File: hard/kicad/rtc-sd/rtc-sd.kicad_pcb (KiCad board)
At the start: 2 copper layers, 53.3 x 130.8 mm, 38 parts, among them J1 SIDECAR, J2 SD0, J3 SD1, J4 SPI2, J5 SPI3, J6 RTC, J7 EXPANSION, Q1 2N7000, U1 74HC138, U2 74HC174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

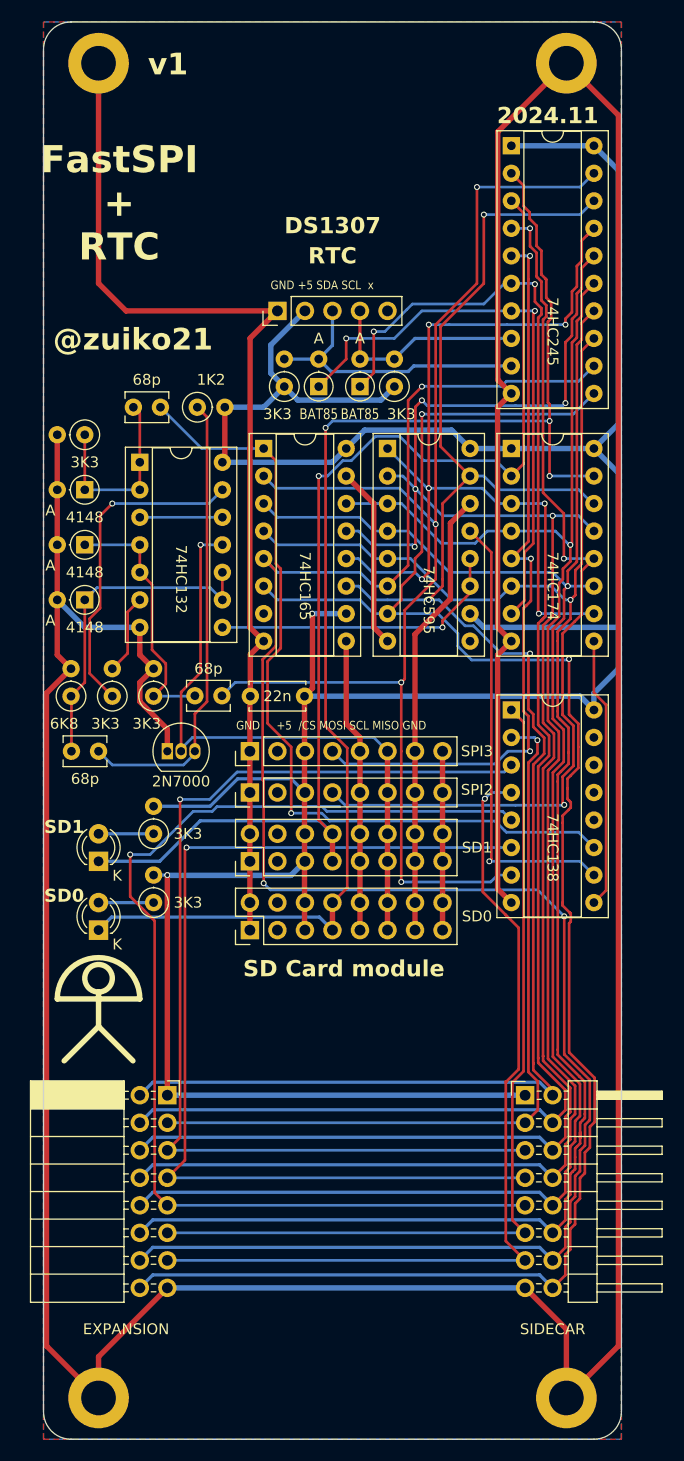
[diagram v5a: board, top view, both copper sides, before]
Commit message: add limits to rtc-sd
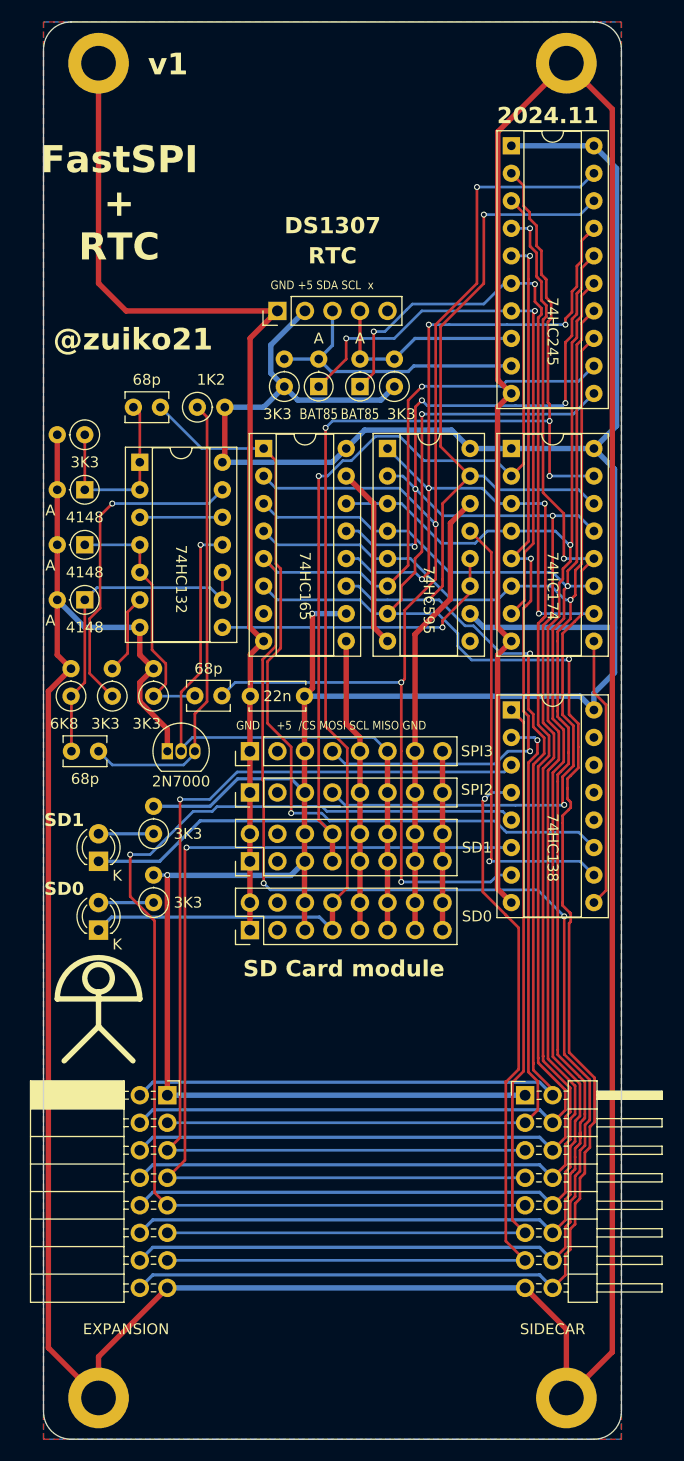
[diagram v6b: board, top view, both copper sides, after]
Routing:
- net +5V: track 288.7 -> 287.9 mm
- net GND: track 512.5 -> 511.8 mm
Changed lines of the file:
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@@
 		)
 		(property "Value" "SD1"
-			(at 3.175 -3.175 0)
+			(at 3.81 -3.175 0)
 			(unlocked yes)
 			(layer "F.SilkS")
@@
 		)
 		(property "Value" "SD0"
-			(at 3.175 -3.175 0)
+			(at 3.81 -3.175 0)
 			(unlocked yes)
 			(layer "F.SilkS")
@@
 	)
 	(segment
-		(start 73.66 152.4)
-		(end 78.465 147.595)
+		(start 68.58 59.69)
+		(end 67.33 58.44)
 		(width 0.5)
 		(layer "F.Cu")
@@
 	)
 	(segment
-		(start 68.58 59.69)
-		(end 67.33 58.44)
+		(start 67.31 60.96)
+		(end 67.31 81.28)
 		(width 0.5)
 		(layer "F.Cu")
@@
 	)
 	(segment
-		(start 67.31 60.96)
-		(end 67.31 81.28)
+		(start 25.85 147.77)
+		(end 25.85 87.18)
 		(width 0.5)
 		(layer "F.Cu")
@@
 	)
 	(segment
-		(start 27.94 85.09)
-		(end 25.675 87.355)
+		(start 25.85 87.18)
+		(end 27.94 85.09)
 		(width 0.5)
 		(layer "F.Cu")
@@
 	)
 	(segment
-		(start 78.465 34.015)
-		(end 73.66 29.21)
+		(start 68.58 59.69)
+		(end 67.31 60.96)
 		(width 0.5)
 		(layer "F.Cu")
@@
 	)
 	(segment
-		(start 68.58 59.69)
-		(end 67.31 60.96)
+		(start 77.9 148.16)
+		(end 77.9 33.45)
 		(width 0.5)
 		(layer "F.Cu")
@@
 	)
 	(segment
-		(start 44.47 54.59)
-		(end 44.47 64.75)
+		(start 30.48 152.4)
+		(end 25.85 147.77)
 		(width 0.5)
 		(layer "F.Cu")
@@
 	)
 	(segment
-		(start 25.675 87.355)
-		(end 25.675 147.595)
+		(start 44.47 54.59)
+		(end 44.47 64.75)
 		(width 0.5)
 		(layer "F.Cu")
@@
 	)
 	(segment
+		(start 77.9 33.45)
+		(end 73.66 29.21)
+		(width 0.5)
+		(layer "F.Cu")
+		(net 1)
+	)
+	(segment
 		(start 73.66 146.05)
 		(end 73.66 152.4)
@@
 	)
 	(segment
-		(start 25.675 147.595)
-		(end 30.48 152.4)
-		(width 0.5)
-		(layer "F.Cu")
-		(net 1)
-	)
-	(segment
 		(start 62.23 109.22)
 		(end 62.23 92.71)
@@
 	)
 	(segment
+		(start 73.66 152.4)
+		(end 77.9 148.16)
+		(width 0.5)
+		(layer "F.Cu")
+		(net 1)
+	)
+	(segment
 		(start 30.48 148.59)
 		(end 30.48 152.4)
@@
 	)
 	(segment
-		(start 78.465 147.595)
-		(end 78.465 34.015)
-		(width 0.5)
-		(layer "F.Cu")
-		(net 1)
-	)
-	(segment
 		(start 68.58 82.55)
 		(end 67.31 83.82)
@@
 	)
 	(segment
-		(start 78.465 39.095)
-		(end 78.465 62.505)
+		(start 50.2 80.01)
+		(end 53.34 80.01)
 		(width 0.5)
 		(layer "B.Cu")
@@
 	)
 	(segment
-		(start 50.2 80.01)
-		(end 53.34 80.01)
+		(start 47.625 59.055)
+		(end 48.875 60.305)
 		(width 0.5)
 		(layer "B.Cu")
@@
 	)
 	(segment
-		(start 47.625 59.055)
-		(end 48.875 60.305)
+		(start 64.77 80.01)
+		(end 66.04 81.28)
 		(width 0.5)
 		(layer "B.Cu")
@@
 	)
 	(segment
-		(start 78.465 62.505)
-		(end 76.2 64.77)
+		(start 76.2 36.83)
+		(end 78.29 38.92)
 		(width 0.5)
 		(layer "B.Cu")
@@
 	)
 	(segment
-		(start 64.77 80.01)
-		(end 66.04 81.28)
-		(width 0.5)
-		(layer "B.Cu")
-		(net 2)
-	)
-	(segment
 		(start 76.2 88.9)
 		(end 74.93 87.63)
@@
 	)
 	(segment
-		(start 47.625 59.055)
-		(end 46.375 57.805)
+		(start 66.04 81.28)
+		(end 78.105 81.28)
 		(width 0.5)
 		(layer "B.Cu")
@@
 	)
 	(segment
-		(start 63.07 63.07)
-		(end 64.77 64.77)
+		(start 47.625 59.055)
+		(end 46.375 57.805)
 		(width 0.5)
 		(layer "B.Cu")
@@
 	)
 	(segment
-		(start 78.465 81.28)
-		(end 78.465 85.09)
+		(start 63.07 63.07)
+		(end 64.77 64.77)
 		(width 0.5)
 		(layer "B.Cu")
@@
 	)
 	(segment
-		(start 76.2 64.77)
-		(end 78.465 67.035)
+		(start 76.2 87.355)
+		(end 76.2 88.9)
 		(width 0.5)
 		(layer "B.Cu")
@@
 	)
 	(segment
-		(start 76.2 36.83)
-		(end 78.465 39.095)
+		(start 48.875 60.305)
+		(end 56.535 60.305)
 		(width 0.5)
 		(layer "B.Cu")
@@
 	)
 	(segment
-		(start 76.2 87.355)
-		(end 76.2 88.9)
+		(start 36.83 104.14)
+		(end 36.86 104.17)
 		(width 0.5)
 		(layer "B.Cu")
@@
 	)
 	(segment
-		(start 48.875 60.305)
-		(end 56.535 60.305)
+		(start 41.91 66.04)
+		(end 52.07 66.04)
 		(width 0.5)
 		(layer "B.Cu")
@@
 	)
 	(segment
-		(start 78.465 85.09)
-		(end 76.2 87.355)
+		(start 78.29 62.68)
+		(end 76.2 64.77)
 		(width 0.5)
 		(layer "B.Cu")
@@
 	)
 	(segment
-		(start 36.83 104.14)
-		(end 36.86 104.17)
+		(start 46.375 57.805)
+		(end 46.375 55.225)
 		(width 0.5)
 		(layer "B.Cu")
@@
 	)
 	(segment
-		(start 41.91 66.04)
-		(end 52.07 66.04)
+		(start 78.105 66.675)
+		(end 78.105 85.45)
 		(width 0.5)
 		(layer "B.Cu")
@@
 	)
 	(segment
-		(start 46.375 57.805)
-		(end 46.375 55.225)
+		(start 52.07 66.04)
+		(end 53.34 64.77)
 		(width 0.5)
 		(layer "B.Cu")
@@
 	)
 	(segment
-		(start 78.465 67.035)
-		(end 78.465 81.28)
+		(start 77.9675 85.5875)
+		(end 76.2 87.355)
 		(width 0.5)
 		(layer "B.Cu")
@@
 	)
 	(segment
-		(start 52.07 66.04)
-		(end 53.34 64.77)
+		(start 76.2 64.77)
+		(end 77.47 66.04)
 		(width 0.5)
 		(layer "B.Cu")
@@
 	)
 	(segment
-		(start 66.04 81.28)
-		(end 78.465 81.28)
+		(start 53.34 64.77)
+		(end 55.04 63.07)
 		(width 0.5)
 		(layer "B.Cu")
@@
 	)
 	(segment
-		(start 53.34 64.77)
-		(end 55.04 63.07)
+		(start 46.375 55.225)
+		(end 49.53 52.07)
 		(width 0.5)
 		(layer "B.Cu")
@@
 	)
 	(segment
-		(start 46.375 55.225)
-		(end 49.53 52.07)
+		(start 77.47 66.04)
+		(end 78.105 66.675)
 		(width 0.5)
 		(layer "B.Cu")
@@
 		(width 0.5)
 		(layer "B.Cu")
+		(net 2)
+	)
+	(segment
+		(start 78.105 85.45)
+		(end 77.9675 85.5875)
+		(width 0.5)
+		(layer "B.Cu")
+		(net 2)
+	)
+	(segment
+		(start 78.29 38.92)
+		(end 78.29 62.68)
+		(width 0.5)
+		(layer "B.Cu")

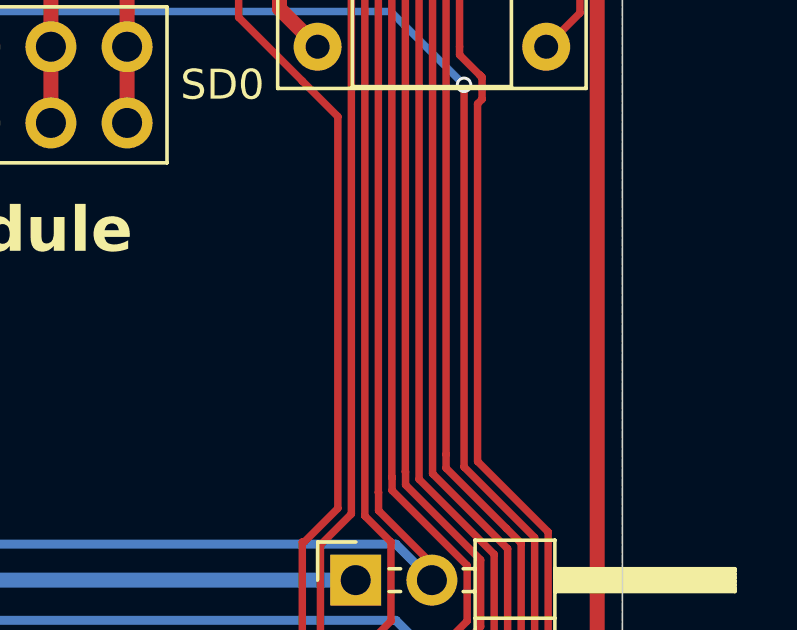
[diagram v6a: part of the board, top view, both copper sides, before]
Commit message: add dron author and J-logo to RTC-SD
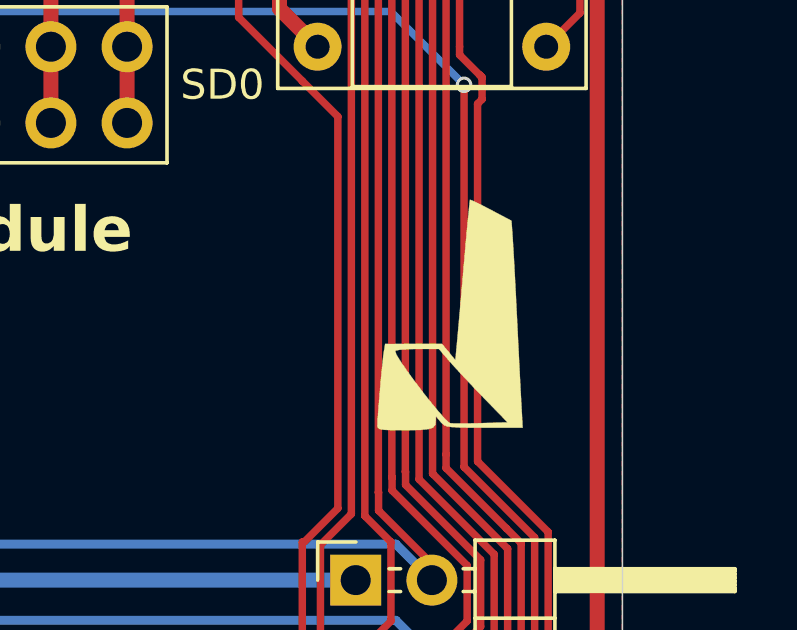
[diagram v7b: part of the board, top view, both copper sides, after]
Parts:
- added LOGO1: Logo_Open_Hardware_Small, durango:j300, F.Cu at (73.0, 115.6)
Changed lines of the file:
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@@
+		)
+	)
+	(footprint "durango:j300"
+		(layer "F.Cu")
+		(at 73.025 115.57)
+		(property "Reference" "LOGO1"
+			(at 0 0 0)
+			(layer "F.SilkS")
+			(hide yes)
+			(effects
+				(font
+					(size 1.524 1.524)
+					(thickness 0.3)
+				)
+			)
+		)
+		(property "Value" "Logo_Open_Hardware_Small"
+			(at 0.75 0 0)
+			(layer "F.SilkS")
+			(hide yes)
+			(effects
+				(font
+					(size 1.524 1.524)
+					(thickness 0.3)
+				)
+			)
+		)
+		(property "Footprint" "durango:j300"
+			(at 0 0 0)
+			(layer "F.Fab")
+			(hide yes)
+			(effects
+				(font
+					(size 1.27 1.27)
+					(thickness 0.15)
+				)
+			)
+		)
+		(property "Datasheet" ""
+			(at 0 0 0)
+			(layer "F.Fab")
+			(hide yes)
+			(effects
+				(font
+					(size 1.27 1.27)
+					(thickness 0.15)
+				)
+			)
+		)
+		(property "Description" ""
+			(at 0 0 0)
+			(layer "F.Fab")
+			(hide yes)
+			(effects
+				(font
+					(size 1.27 1.27)
+					(thickness 0.15)
+				)
+			)
+		)
+		(sheetname "Root")
+		(sheetfile "rtc-sd.kicad_sch")
+		(attr through_hole)
+		(fp_poly
+			(pts
+				(xy 0.710652 -3.763118) (xy 0.903066 -3.672452) (xy 1.176324 -3.534458) (xy 1.335497 -3.451331)
+				(xy 2.019553 -3.090333) (xy 2.065245 -2.413) (xy 2.083451 -2.118304) (xy 2.107502 -1.692574) (xy 2.135359 -1.173928)
+				(xy 2.164981 -0.600482) (xy 2.194328 -0.010352) (xy 2.198938 0.084667) (xy 2.228922 0.698733) (xy 2.260059 1.325668)
+				(xy 2.29009 1.920723) (xy 2.316755 2.439151) (xy 2.337794 2.836202) (xy 2.338955 2.8575) (xy 2.390969 3.81)
+				(xy 1.103222 3.81) (xy 0.608986 3.808781) (xy 0.255761 3.802636) (xy 0.015232 3.787837) (xy -0.140919 3.760655)
+				(xy -0.241009 3.717362) (xy -0.313354 3.654229) (xy -0.343446 3.6195) (xy -0.502367 3.429) (xy -0.505184 3.610442)
+				(xy -0.525357 3.727391) (xy -0.599029 3.807525) (xy -0.752334 3.857532) (xy -1.011408 3.884102)
+				(xy -1.402385 3.893926) (xy -1.615592 3.894667) (xy -2.00159 3.891566) (xy -2.248365 3.878726) (xy -2.385966 3.850838)
+				(xy -2.444445 3.802595) (xy -2.45446 3.7465) (xy -2.44595 3.561746) (xy -2.424264 3.252695) (xy -2.393266 2.863522)
+				(xy -2.356817 2.438404) (xy -2.318778 2.021518) (xy -2.283012 1.657041) (xy -2.25338 1.389148) (xy -2.239821 1.291167)
+				(xy -2.233738 1.254904) (xy -1.862667 1.254904) (xy -1.811943 1.379807) (xy -1.674065 1.604827)
+				(xy -1.470477 1.901954) (xy -1.222622 2.243181) (xy -0.951945 2.600499) (xy -0.679888 2.9459) (xy -0.427895 3.251375)
+				(xy -0.21741 3.488916) (xy -0.069875 3.630515) (xy -0.023325 3.657353) (xy 0.111304 3.665583) (xy 0.373177 3.66747)
+				(xy 0.720324 3.663061) (xy 0.994002 3.656183) (xy 1.883259 3.629365) (xy 1.08654 2.809516) (xy 0.753544 2.463296)
+				(xy 0.428931 2.119564) (xy 0.148995 1.817128) (xy -0.04997 1.594798) (xy -0.056264 1.5875) (xy -0.402349 1.185334)
+				(xy -1.132508 1.185334) (xy -1.460314 1.192786) (xy -1.711913 1.212693) (xy -1.848718 1.241377)
+				(xy -1.862667 1.254904) (xy -2.233738 1.254904) (xy -2.193661 1.016) (xy -1.244997 1.015237) (xy -0.296334 1.014474)
+				(xy -0.074928 1.283842) (xy 0.146478 1.553211) (xy 0.197558 1.009439) (xy 0.219278 0.771488) (xy 0.252799 0.395776)
+				(xy 0.295393 -0.086745) (xy 0.344337 -0.645129) (xy 0.396905 -1.248424) (xy 0.431814 -1.651) (xy 0.48255 -2.23009)
+				(xy 0.529337 -2.750515) (xy 0.570022 -3.189407) (xy 0.602451 -3.523898) (xy 0.624471 -3.731121)
+				(xy 0.633215 -3.789998) (xy 0.710652 -3.763118)
+			)
+			(stroke
+				(width 0.01)
+				(type solid)
+			)
+			(fill solid)
+			(layer "F.SilkS")
 		)
 	)

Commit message: fix silcreen on triPSG, ready for order
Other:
- board text added: "JLCJLCJLCJLC"
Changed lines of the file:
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@@
 			(plot_on_all_layers_selection 0x0000000_00000000)
 			(disableapertmacros no)
-			(usegerberextensions no)
-			(usegerberattributes yes)
-			(usegerberadvancedattributes yes)
-			(creategerberjobfile yes)
+			(usegerberextensions yes)
+			(usegerberattributes no)
+			(usegerberadvancedattributes no)
+			(creategerberjobfile no)
 			(dashed_line_dash_ratio 12.000000)
 			(dashed_line_gap_ratio 3.000000)
@@
 			(plotinvisibletext no)
 			(sketchpadsonfab no)
-			(subtractmaskfromsilk no)
+			(subtractmaskfromsilk yes)
 			(outputformat 1)
 			(mirror no)
-			(drillshape 1)
+			(drillshape 0)
 			(scaleselection 1)
-			(outputdirectory "")
+			(outputdirectory "gerber/")
 		)
 	)
@@
 		(layer "Edge.Cuts")
 	)
+	(gr_text "JLCJLCJLCJLC"
+		(at 58.166 154.813 0)
+		(layer "B.SilkS")
+		(effects
+			(font
+				(size 1 1)
+				(thickness 0.15)
+			)
+			(justify left bottom mirror)
+		)
+	)
 	(gr_text "FastSPI\n+\nRTC"
